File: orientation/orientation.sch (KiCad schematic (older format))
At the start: 5 parts, among them J1 Conn_01x02, J2 Conn_01x04, U1 Teensy4.0, U2 STSPIN220, U3 bno055

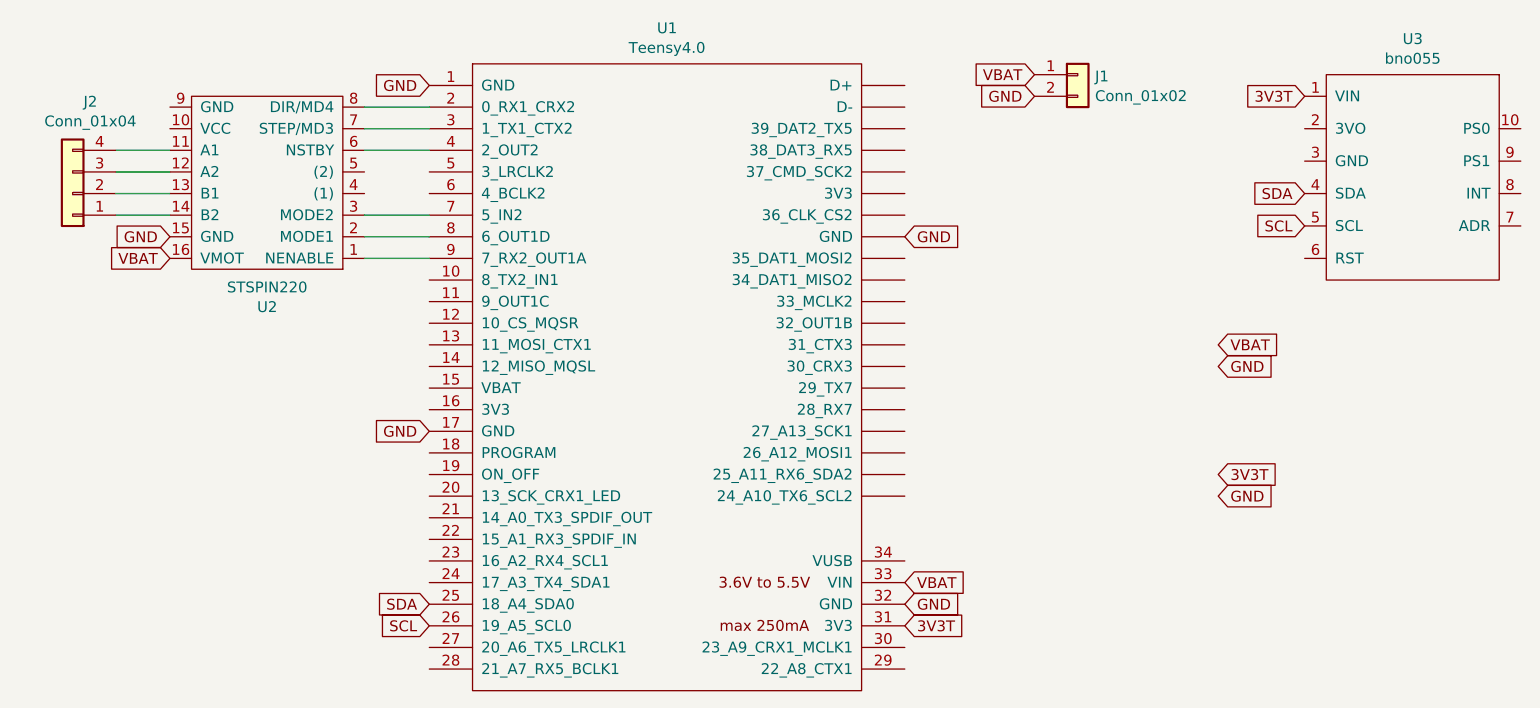
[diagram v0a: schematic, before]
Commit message: add switch to orientation board
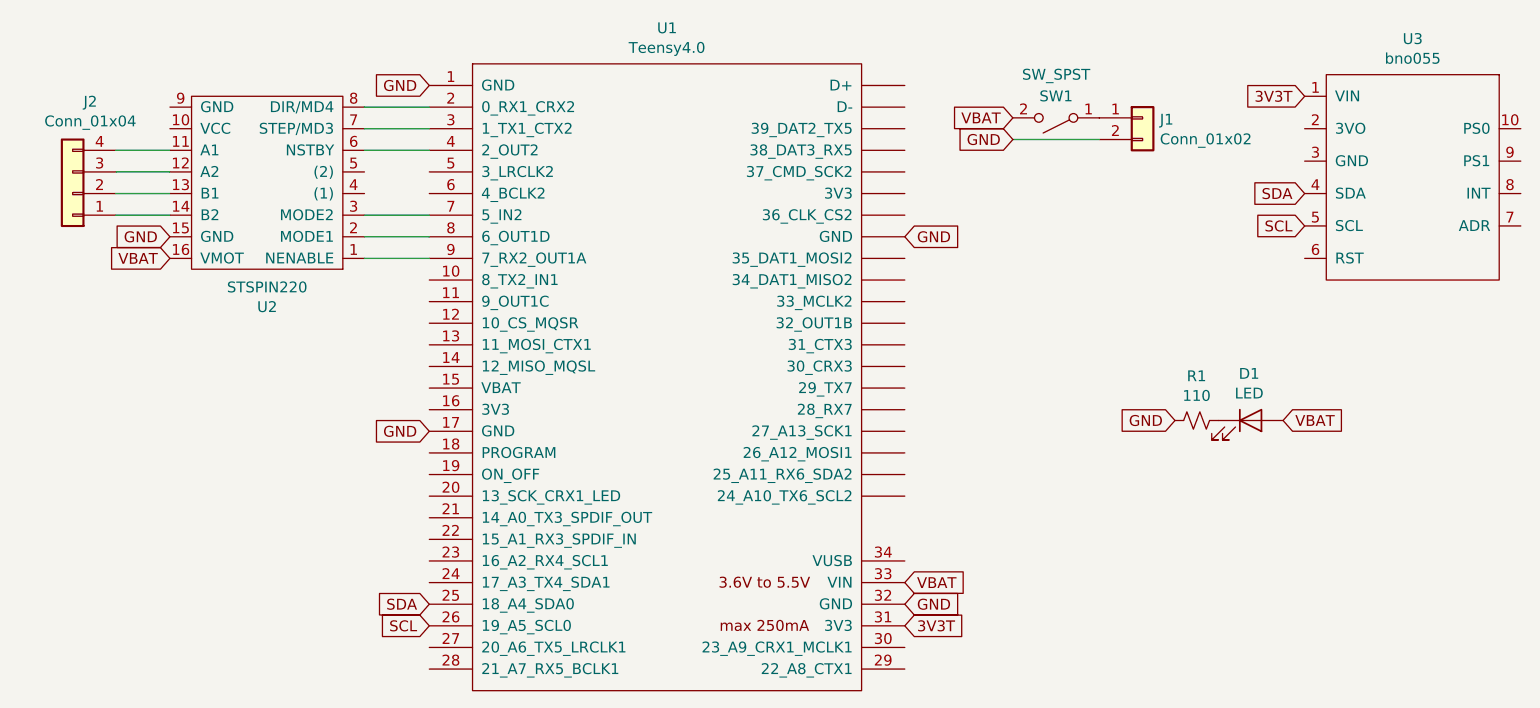
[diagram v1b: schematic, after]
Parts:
- added D1: LED, LED_SMD:LED_1206_3216Metric_Pad1.42x1.75mm_HandSolder, symbol Device:LED
- added R1: 110, Resistor_SMD:R_1206_3216Metric_Pad1.42x1.75mm_HandSolder, symbol Device:R_Small_US
- added SW1: SW_SPST, NUSTARS:GF-123-0054, symbol Switch:SW_SPST
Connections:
- net GND: now also R1.2
- net VBAT: now also D1.2 (A), SW1.2 (B); no longer J1.1 (Pin_1)
- new net: J1.1 (Pin_1), SW1.1 (A)
- new net: D1.1 (K), R1.1
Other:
- moved on the sheet: J1
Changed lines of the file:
@@
 L Connector_Generic:Conn_01x02 J1
 U 1 1 5E1EFEDF
-P 5400 2300
-F 0 "J1" H 5480 2292 50  0000 L CNN
-F 1 "Conn_01x02" H 5480 2201 50  0000 L CNN
-F 2 "Connector_JST:JST_PH_B2B-PH-K_1x02_P2.00mm_Vertical" H 5400 2300 50  0001 C CNN
-F 3 "~" H 5400 2300 50  0001 C CNN
-	1    5400 2300
+P 5700 2500
+F 0 "J1" H 5780 2492 50  0000 L CNN
+F 1 "Conn_01x02" H 5780 2401 50  0000 L CNN
+F 2 "Connector_JST:JST_PH_B2B-PH-K_1x02_P2.00mm_Vertical" H 5700 2500 50  0001 C CNN
+F 3 "~" H 5700 2500 50  0001 C CNN
+	1    5700 2500
 	1    0    0    -1
 $EndComp
@@
 Text GLabel 2400 4750 0    50   Input ~ 0
 SDA
-Text GLabel 5200 2300 0    50   Input ~ 0
+Text GLabel 5100 2500 0    50   Input ~ 0
 VBAT
-Text GLabel 5200 2400 0    50   Input ~ 0
+Text GLabel 5100 2600 0    50   Input ~ 0
 GND
 Text GLabel 4600 4850 2    50   Input ~ 0
 3V3T
-Text GLabel 6050 3650 2    50   Input ~ 0
-GND
-Text GLabel 6050 4250 2    50   Input ~ 0
-GND
-Text GLabel 6050 4150 2    50   Input ~ 0
-3V3T
-Text GLabel 6050 3550 2    50   Input ~ 0
-VBAT
 Text GLabel 6450 2400 0    50   Input ~ 0
 3V3T
@@
 Wire Wire Line
 	950  2950 1200 2950
+$Comp
+L Switch:SW_SPST SW1
+U 1 1 5E1530D8
+P 5300 2500
+F 0 "SW1" H 5300 2400 50  0000 C CNN
+F 1 "SW_SPST" H 5300 2300 50  0000 C CNN
+F 2 "NUSTARS:GF-123-0054" H 5300 2500 50  0001 C CNN
+F 3 "~" H 5300 2500 50  0001 C CNN
+	1    5300 2500
+	-1   0    0    1
+$EndComp
+Wire Wire Line
+	5500 2600 5100 2600
+$Comp
+L Device:LED D1
+U 1 1 5E15F99C
+P 6200 3900
+F 0 "D1" H 6193 4116 50  0000 C CNN
+F 1 "LED" H 6193 4025 50  0000 C CNN
+F 2 "LED_SMD:LED_1206_3216Metric_Pad1.42x1.75mm_HandSolder" H 6200 3900 50  0001 C CNN
+F 3 "~" H 6200 3900 50  0001 C CNN
+	1    6200 3900
+	1    0    0    -1
+$EndComp
+Text GLabel 6350 3900 2    50   Input ~ 0
+VBAT
+$Comp
+L Device:R_Small_US R1
+U 1 1 5E163AC3
+P 5950 3900
+F 0 "R1" V 5745 3900 50  0000 C CNN
+F 1 "110" V 5836 3900 50  0000 C CNN
+F 2 "Resistor_SMD:R_1206_3216Metric_Pad1.42x1.75mm_HandSolder" H 5950 3900 50  0001 C CNN
+F 3 "~" H 5950 3900 50  0001 C CNN
+	1    5950 3900
+	0    1    1    0
+$EndComp
+Text GLabel 5850 3900 0    50   Input ~ 0
+GND
 $EndSCHEMATC

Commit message: misc changes
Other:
- moved on the sheet: D1, J1, R1, SW1, U3
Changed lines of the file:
@@
 L NUSTARS:bno055 U3
 U 1 1 5E1EF17C
-P 6550 2300
-F 0 "U3" H 6950 2465 50  0000 C CNN
-F 1 "bno055" H 6950 2374 50  0000 C CNN
-F 2 "NUSTARS:bno055" H 6900 2450 50  0001 C CNN
-F 3 "" H 6900 2450 50  0001 C CNN
-	1    6550 2300
+P 5300 3750
+F 0 "U3" H 5700 3915 50  0000 C CNN
+F 1 "bno055" H 5700 3824 50  0000 C CNN
+F 2 "NUSTARS:bno055" H 5650 3900 50  0001 C CNN
+F 3 "" H 5650 3900 50  0001 C CNN
+	1    5300 3750
 	1    0    0    -1
 $EndComp
@@
 L Connector_Generic:Conn_01x02 J1
 U 1 1 5E1EFEDF
-P 5700 2500
-F 0 "J1" H 5780 2492 50  0000 L CNN
-F 1 "Conn_01x02" H 5780 2401 50  0000 L CNN
-F 2 "Connector_JST:JST_PH_B2B-PH-K_1x02_P2.00mm_Vertical" H 5700 2500 50  0001 C CNN
-F 3 "~" H 5700 2500 50  0001 C CNN
-	1    5700 2500
+P 5650 2650
+F 0 "J1" H 5730 2642 50  0000 L CNN
+F 1 "Conn_01x02" H 5730 2551 50  0000 L CNN
+F 2 "Connector_JST:JST_PH_B2B-PH-K_1x02_P2.00mm_Vertical" H 5650 2650 50  0001 C CNN
+F 3 "~" H 5650 2650 50  0001 C CNN
+	1    5650 2650
 	1    0    0    -1
 $EndComp
@@
 Text GLabel 2400 4750 0    50   Input ~ 0
 SDA
-Text GLabel 5100 2500 0    50   Input ~ 0
+Text GLabel 5050 2650 0    50   Input ~ 0
 VBAT
-Text GLabel 5100 2600 0    50   Input ~ 0
+Text GLabel 5050 2750 0    50   Input ~ 0
 GND
 Text GLabel 4600 4850 2    50   Input ~ 0
 3V3T
-Text GLabel 6450 2400 0    50   Input ~ 0
+Text GLabel 5200 3850 0    50   Input ~ 0
 3V3T
-Text GLabel 6450 2850 0    50   Input ~ 0
+Text GLabel 5200 4300 0    50   Input ~ 0
 SDA
-Text GLabel 6450 3000 0    50   Input ~ 0
+Text GLabel 5200 4450 0    50   Input ~ 0
 SCL
 Text GLabel 2400 2350 0    50   Input ~ 0
@@
 L Switch:SW_SPST SW1
 U 1 1 5E1530D8
-P 5300 2500
-F 0 "SW1" H 5300 2400 50  0000 C CNN
-F 1 "SW_SPST" H 5300 2300 50  0000 C CNN
-F 2 "NUSTARS:GF-123-0054" H 5300 2500 50  0001 C CNN
-F 3 "~" H 5300 2500 50  0001 C CNN
-	1    5300 2500
+P 5250 2650
+F 0 "SW1" H 5250 2550 50  0000 C CNN
+F 1 "SW_SPST" H 5250 2450 50  0000 C CNN
+F 2 "NUSTARS:GF-123-0054" H 5250 2650 50  0001 C CNN
+F 3 "~" H 5250 2650 50  0001 C CNN
+	1    5250 2650
 	-1   0    0    1
 $EndComp
 Wire Wire Line
-	5500 2600 5100 2600
+	5450 2750 5050 2750
 $Comp
 L Device:LED D1
 U 1 1 5E15F99C
-P 6200 3900
-F 0 "D1" H 6193 4116 50  0000 C CNN
-F 1 "LED" H 6193 4025 50  0000 C CNN
-F 2 "LED_SMD:LED_1206_3216Metric_Pad1.42x1.75mm_HandSolder" H 6200 3900 50  0001 C CNN
-F 3 "~" H 6200 3900 50  0001 C CNN
-	1    6200 3900
+P 5500 3350
+F 0 "D1" H 5493 3566 50  0000 C CNN
+F 1 "LED" H 5493 3475 50  0000 C CNN
+F 2 "LED_SMD:LED_1206_3216Metric_Pad1.42x1.75mm_HandSolder" H 5500 3350 50  0001 C CNN
+F 3 "~" H 5500 3350 50  0001 C CNN
+	1    5500 3350
 	1    0    0    -1
 $EndComp
-Text GLabel 6350 3900 2    50   Input ~ 0
+Text GLabel 5650 3350 2    50   Input ~ 0
 VBAT
 $Comp
 L Device:R_Small_US R1
 U 1 1 5E163AC3
-P 5950 3900
-F 0 "R1" V 5745 3900 50  0000 C CNN
-F 1 "110" V 5836 3900 50  0000 C CNN
-F 2 "Resistor_SMD:R_1206_3216Metric_Pad1.42x1.75mm_HandSolder" H 5950 3900 50  0001 C CNN
-F 3 "~" H 5950 3900 50  0001 C CNN
-	1    5950 3900
+P 5250 3350
+F 0 "R1" V 5045 3350 50  0000 C CNN
+F 1 "110" V 5136 3350 50  0000 C CNN
+F 2 "Resistor_SMD:R_1206_3216Metric_Pad1.42x1.75mm_HandSolder" H 5250 3350 50  0001 C CNN
+F 3 "~" H 5250 3350 50  0001 C CNN
+	1    5250 3350
 	0    1    1    0
 $EndComp
-Text GLabel 5850 3900 0    50   Input ~ 0
+Text GLabel 5150 3350 0    50   Input ~ 0
 GND
 $EndSCHEMATC

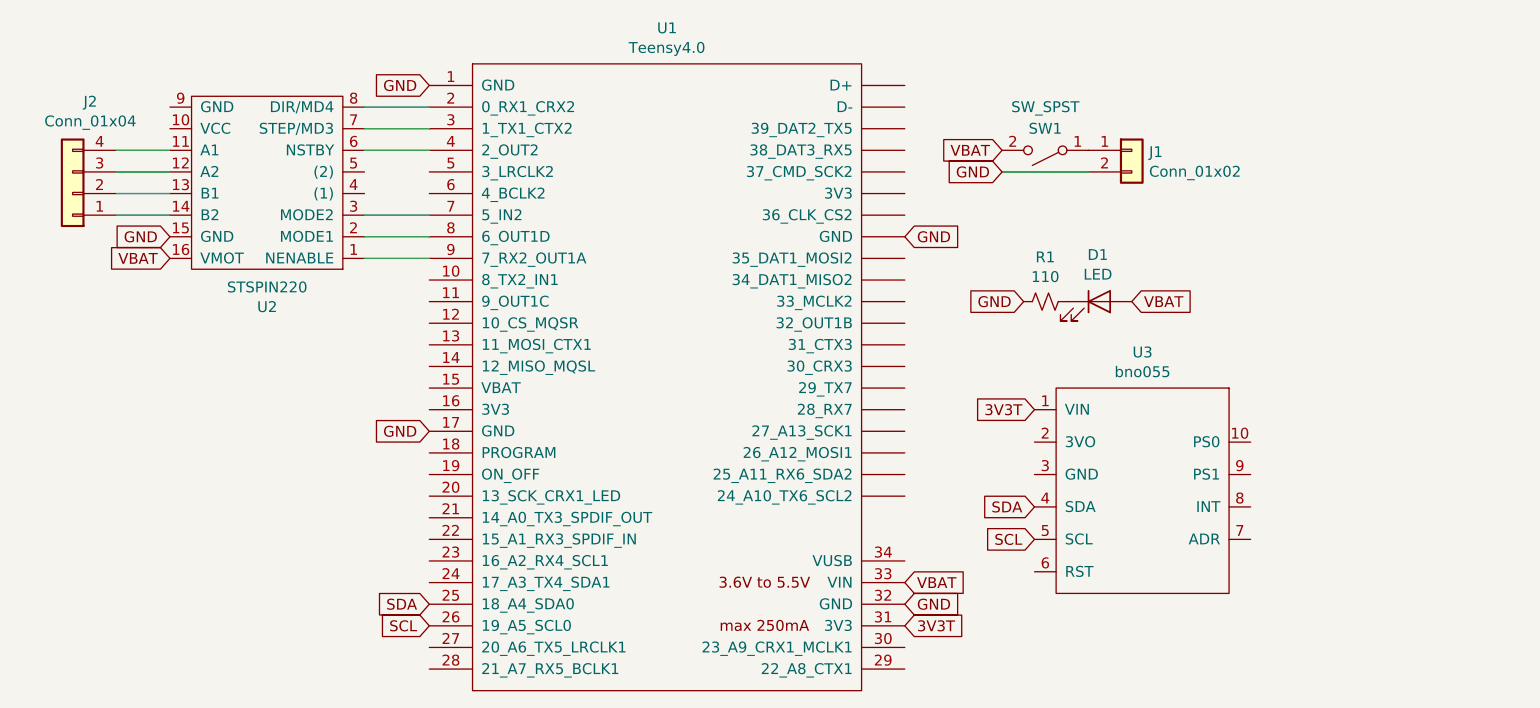
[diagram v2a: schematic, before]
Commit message: add GND and 3.3V connections on orientation
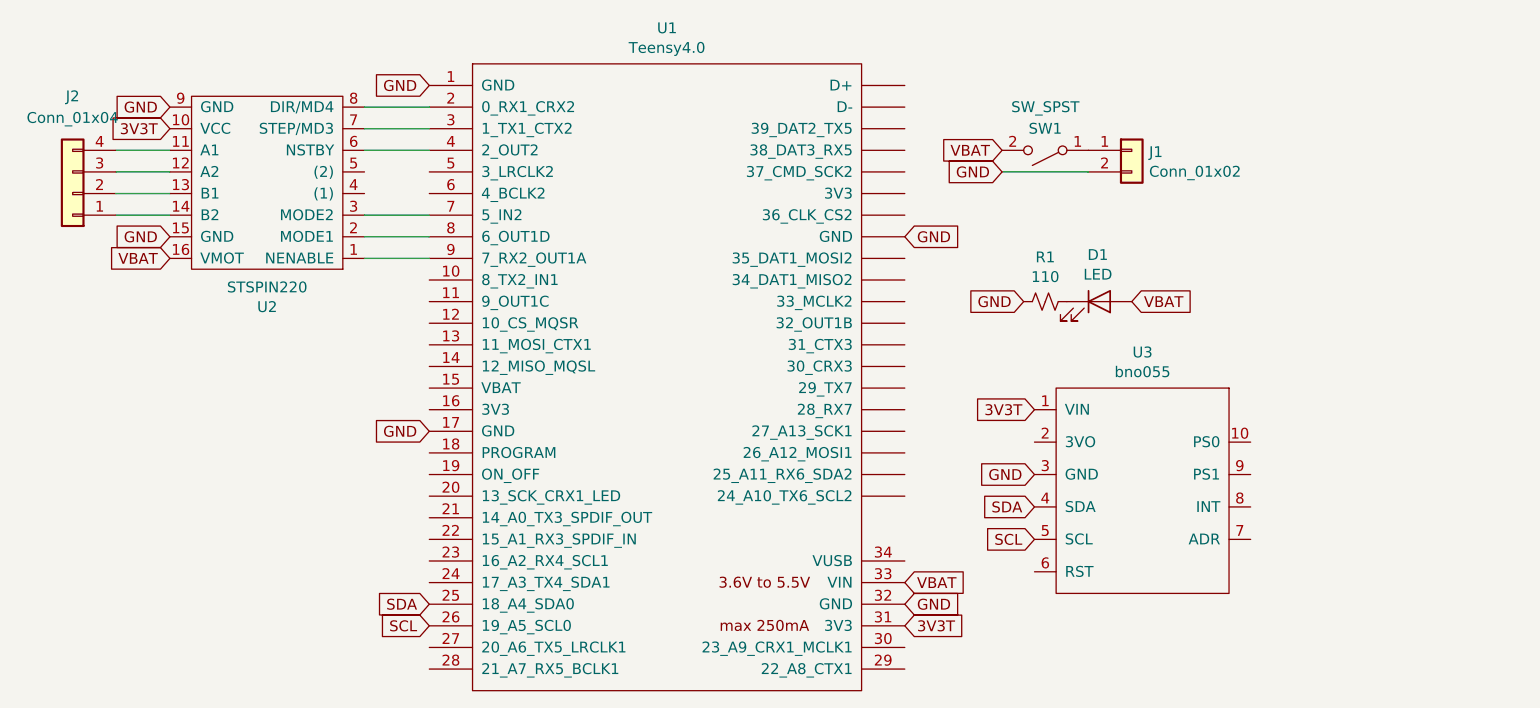
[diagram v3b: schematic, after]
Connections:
- net 3V3T: now also U2.10 (VCC)
- net GND: now also U2.9 (GND), U3.3 (GND)
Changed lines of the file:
@@
 EESchema Schematic File Version 4
+LIBS:orientation-cache
 EELAYER 30 0
 EELAYER END
@@
 	1    0    0    -1
 $EndComp
-$Comp
-L NUSTARS:STSPIN220 U2
-U 1 1 5E1F3164
-P 2000 3200
-F 0 "U2" H 2350 3375 50  0000 C CNN
-F 1 "STSPIN220" H 2350 3284 50  0000 C CNN
-F 2 "NUSTARS:STSPIN220" H 2350 3350 50  0001 C CNN
-F 3 "" H 2350 3350 50  0001 C CNN
-	1    2000 3200
-	-1   0    0    1
-$EndComp
 Text GLabel 2400 4850 0    50   Input ~ 0
 SCL
@@
 U 1 1 5E23630E
 P 750 2850
-F 0 "J2" H 668 2425 50  0000 C CNN
-F 1 "Conn_01x04" H 668 2516 50  0000 C CNN
+F 0 "J2" H 750 2400 50  0000 C CNN
+F 1 "Conn_01x04" H 750 2500 50  0000 C CNN
 F 2 "Connector_JST:JST_PH_B4B-PH-K_1x04_P2.00mm_Vertical" H 750 2850 50  0001 C CNN
 F 3 "~" H 750 2850 50  0001 C CNN
@@
 Text GLabel 5150 3350 0    50   Input ~ 0
 GND
+$Comp
+L NUSTARS:STSPIN220 U2
+U 1 1 5E1F3164
+P 2000 3200
+F 0 "U2" H 2350 3375 50  0000 C CNN
+F 1 "STSPIN220" H 2350 3284 50  0000 C CNN
+F 2 "NUSTARS:STSPIN220" H 2350 3350 50  0001 C CNN
+F 3 "" H 2350 3350 50  0001 C CNN
+	1    2000 3200
+	-1   0    0    1
+$EndComp
+Text GLabel 1200 2450 0    50   Input ~ 0
+GND
+Text GLabel 1200 2550 0    50   Input ~ 0
+3V3T
+Text GLabel 5200 4150 0    50   Input ~ 0
+GND
 $EndSCHEMATC
